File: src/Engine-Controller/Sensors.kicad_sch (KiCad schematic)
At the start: 30 parts, among them P16 647676-2, P17 0530470410, P8 20021511-00026T4LF, U12 MAX4617EUE+T, U13 MAX4617EUE+T, U14 MCP96L01T-E_MX, U15 AD623ARZ-R7, U7 MC74HC4066ADG, U8 AD623ARZ-R7, U9 MC74HC4066ADG

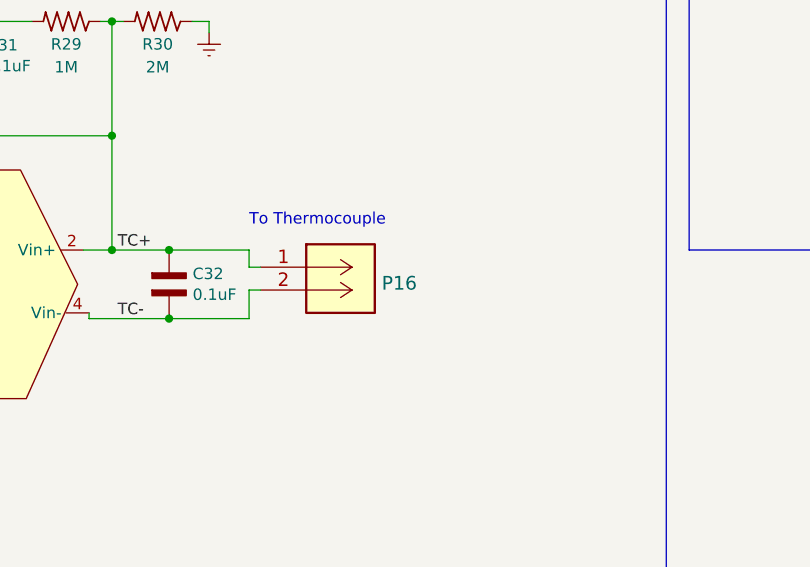
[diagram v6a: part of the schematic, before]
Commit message: changed TC connector to be different from power connector
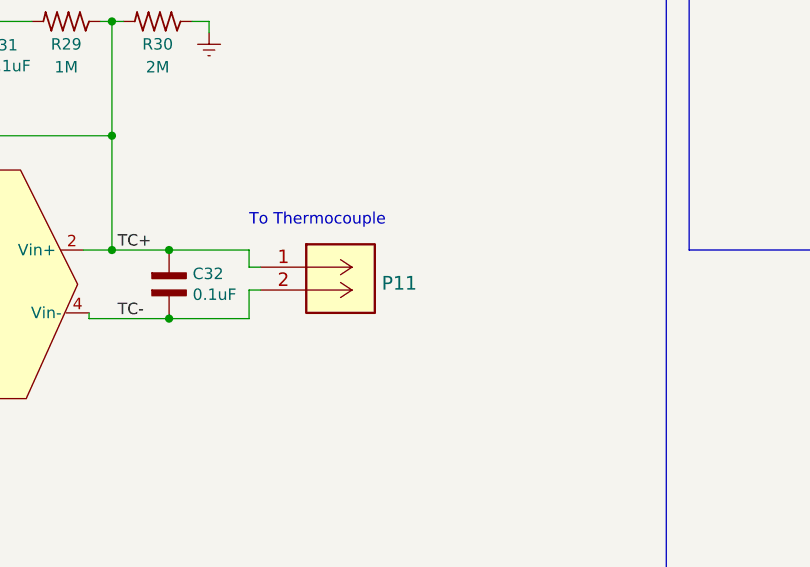
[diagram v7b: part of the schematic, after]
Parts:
- removed P16: 647676-2, Engine-Controller:647676-2, symbol Engine-Controller:647676-2
- added P11: 532580229, Engine-Controller:532580229, symbol Engine-Controller:532580229
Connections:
- net TC+: now also P11.1
- net TC-: now also P11.2
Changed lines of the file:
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@@
+    (pin "2")
+  )
+  (symbol (lib_id "Engine-Controller:532580229") (at 128.905 161.29 0) (unit 1)
+    (in_bom yes) (on_board yes) (fields_autoplaced)
+    (property "Reference" "P11" (id 0) (at 142.367 163.0805 0)
+      (effects (font (size 1.524 1.524)) (justify left))
+    )
+    (property "Value" "532580229" (id 1) (at 137.795 172.72 0)
+      (effects (font (size 1.524 1.524)) hide)
+    )
+    (property "Footprint" "Engine-Controller:532580229" (id 2) (at 137.795 175.26 0)
+      (effects (font (size 1.524 1.524)) hide)
+    )
+    (property "Datasheet" "" (id 3) (at 128.905 161.29 0)
+      (effects (font (size 1.524 1.524)) hide)
+    )
+    (pin "1")
     (pin "2")
   )
@@
     (pin "7")
   )
-  (symbol (lib_id "Engine-Controller:647676-2") (at 128.905 161.29 0) (unit 1)
-    (in_bom yes) (on_board yes) (fields_autoplaced)
-    (property "Reference" "P16" (id 0) (at 142.367 163.0805 0)
-      (effects (font (size 1.524 1.524)) (justify left))
-    )
-    (property "Value" "647676-2" (id 1) (at 137.795 172.72 0)
-      (effects (font (size 1.524 1.524)) hide)
-    )
-    (property "Footprint" "Engine-Controller:647676-2" (id 2) (at 137.795 175.26 0)
-      (effects (font (size 1.524 1.524)) hide)
-    )
-    (property "Datasheet" "" (id 3) (at 128.905 161.29 0)
-      (effects (font (size 1.524 1.524)) hide)
-    )
-    (pin "1")
-    (pin "2")
-  )
   (symbol (lib_id "Engine-Controller:MC74HC4066ADG") (at 231.775 55.88 90) (unit 1)
